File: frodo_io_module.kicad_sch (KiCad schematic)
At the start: 150 parts, among them J1 Conn_02x04_Top_Bottom, J10 JST-GH 4Pin, J11 JST-GH 4Pin, J14 Conn_02x03_Odd_Even, J16 USB_C_Receptacle_USB2.0, J17 TC2050, J2 Conn_02x10_Odd_Even, J3 Conn_02x04_Top_Bottom, J4 Conn_02x03_Odd_Even, J5 Conn_02x04_Odd_Even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

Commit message: more routing
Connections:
- net v_main_pre_sense is gone; now on net main_voltage: D13.1 (K), D14.1 (K)
- net AIN2: now also U3.25 (PC5); no longer U3.24 (PC4)
- net AIN3: now also U3.24 (PC4); no longer U3.25 (PC5)
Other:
- note added: "@todo: swaped AIN2 und AIN3 for better routing"
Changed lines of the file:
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@@
 		)
 	)
+	(text "@todo: swaped AIN2 und AIN3 for better routing"
+		(exclude_from_sim no)
+		(at 261.62 89.408 0)
+		(effects
+			(font
+				(size 1.27 1.27)
+			)
+		)
+	)
 	(text "Isense"
 		(exclude_from_sim no)
@@
 	(global_label "AIN3"
 		(shape input)
-		(at 299.72 82.55 180)
+		(at 299.72 80.01 180)
 		(fields_autoplaced yes)
 		(effects
@@
 		)
 		(property "Intersheetrefs" "${INTERSHEET_REFS}"
-			(at 292.5014 82.55 0)
+			(at 292.5014 80.01 0)
 			(effects
 				(font
@@
 	(global_label "AIN2"
 		(shape input)
-		(at 299.72 80.01 180)
+		(at 299.72 82.55 180)
 		(fields_autoplaced yes)
 		(effects
@@
 		)
 		(property "Intersheetrefs" "${INTERSHEET_REFS}"
-			(at 292.5014 80.01 0)
+			(at 292.5014 82.55 0)
 			(effects
 				(font
@@
 			)
 		)
-		(property "Value" "v_main_pre_sense"
+		(property "Value" "main_voltage"
 			(at 60.96 172.7199 90)
 			(effects

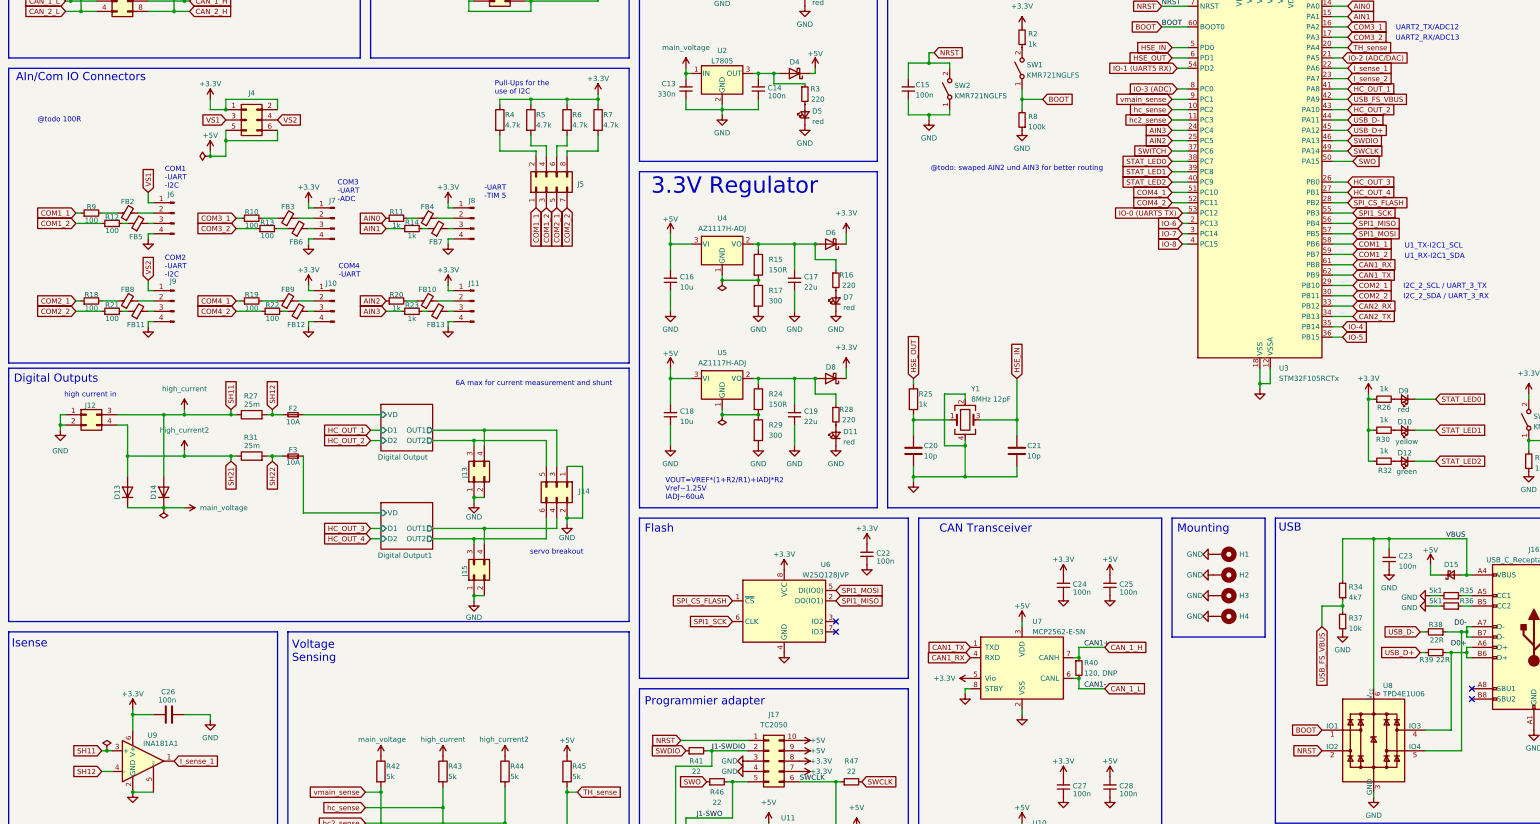
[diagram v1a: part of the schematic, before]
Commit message: remove second 3.3V reg and i2c pull up jumpers
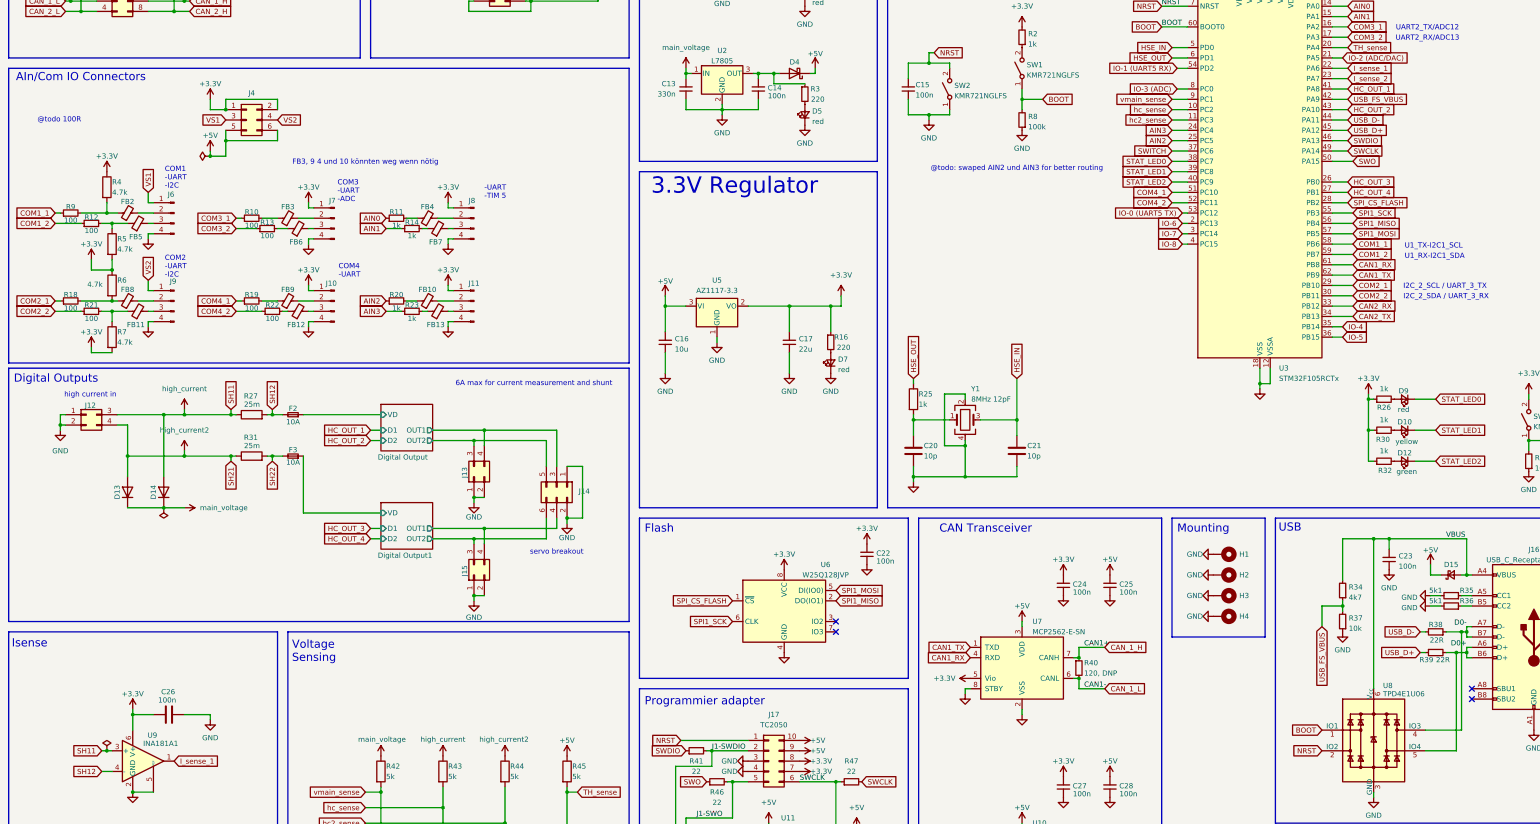
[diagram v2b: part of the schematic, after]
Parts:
- removed C18: 10u, Capacitor_SMD:C_0402_1005Metric, symbol Device:C_Small
- removed C19: 22u, Capacitor_SMD:C_0402_1005Metric, symbol Device:C_Small
- removed D11: red, LED_SMD:LED_0603_1608Metric, symbol Device:LED_Small
- removed D6, D8: RB070MM-30TR, Diode_SMD:D_SOD-123F, symbol Diode:SS34
- removed J5: Conn_02x04_Odd_Even, Connector_PinHeader_1.27mm:PinHeader_2x04_P1.27mm_Vertical_SMD, symbol Connector_Generic:Conn_02x04_Odd_Even
- removed R15, R24: 150R, Resistor_SMD:R_0402_1005Metric, symbol Device:R
- removed R17, R29: 300, Resistor_SMD:R_0402_1005Metric, symbol Device:R
- removed R28: 220, Resistor_SMD:R_0402_1005Metric, symbol Device:R_Small
- removed U4: AZ1117H-ADJ, Package_TO_SOT_SMD:SOT-223-3_TabPin2, symbol Regulator_Linear:AZ1117-3.3
- J14: footprint Connector_PinHeader_2.54mm:PinHeader_2x03_P2.54mm_Vertical_SMD -> Connector_PinHeader_2.54mm:PinHeader_2x03_P2.54mm_Vertical
- U5: value AZ1117H-ADJ -> AZ1117-3.3; LCSC C110475 -> C92102; Manufacturer Diodes Incorporated -> (none); Part# Diodes Incorporated AZ1117H-ADJTRG1 -> (none)
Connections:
- net +3.3V: now also C17.2, R16.1, R5.2, R7.2, U5.2 (VO); no longer R5.1, R7.1
- net D0+: now also U8.5 (IO4); no longer U8.4 (IO3)
- net D0-: now also U8.4 (IO3); no longer U8.5 (IO4)
- net GND: now also U5.1 (GND)
- net at R4.2: now also FB2.1, R9.2
- net at R6.2: now also FB8.1, R18.2
- net at FB11.1, R21.2: now also R7.1
- net at FB5.1, R12.2: now also R5.1
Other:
- note added: "FB3, 9 4 und 10 könnten weg wenn nötig"
- note removed: "Pull-Ups for the use of I2C"
- note removed: "VOUT=VREF*(1+R2/R1)+IADJ*R2 Vref~1.25V IADJ~60uA"
- moved on the sheet: C16, C17, D7, R12, R16, R18, R21, R4, R5, R6, R7, R9

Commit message: more routing
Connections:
- net AIN0: now also U3.23 (PA7); no longer U3.14 (PA0)
- net AIN1: now also U3.22 (PA6); no longer U3.15 (PA1)
- net I_sense_1: now also U3.14 (PA0); no longer U3.22 (PA6)
- net I_sense_2: now also U3.15 (PA1); no longer U3.23 (PA7)
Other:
- note added: "14, 15 mit 22, 23 getauscht"
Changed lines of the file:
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@@
 		)
 	)
+	(text "14, 15 mit 22, 23 getauscht"
+		(exclude_from_sim no)
+		(at 387.604 52.324 0)
+		(effects
+			(font
+				(size 1.27 1.27)
+			)
+		)
+	)
 	(text "COM3\n-UART\n-ADC"
 		(exclude_from_sim no)
@@
 	(global_label "I_sense_1"
 		(shape input)
-		(at 342.9 64.77 0)
+		(at 342.9 49.53 0)
 		(fields_autoplaced yes)
 		(effects
@@
 		)
 		(property "Intersheetrefs" "${INTERSHEET_REFS}"
-			(at 355.0171 64.77 0)
+			(at 355.0171 49.53 0)
 			(effects
 				(font
@@
 	(global_label "AIN1"
 		(shape input)
-		(at 342.9 52.07 0)
+		(at 342.9 64.77 0)
 		(fields_autoplaced yes)
 		(effects
@@
 		)
 		(property "Intersheetrefs" "${INTERSHEET_REFS}"
-			(at 350.1186 52.07 0)
+			(at 350.1186 64.77 0)
 			(effects
 				(font
@@
 	(global_label "AIN0"
 		(shape input)
-		(at 342.9 49.53 0)
+		(at 342.9 67.31 0)
 		(fields_autoplaced yes)
 		(effects
@@
 		)
 		(property "Intersheetrefs" "${INTERSHEET_REFS}"
-			(at 350.1186 49.53 0)
+			(at 350.1186 67.31 0)
 			(effects
 				(font
@@
 	(global_label "I_sense_2"
 		(shape input)
-		(at 342.9 67.31 0)
+		(at 342.9 52.07 0)
 		(fields_autoplaced yes)
 		(effects
@@
 		)
 		(property "Intersheetrefs" "${INTERSHEET_REFS}"
-			(at 355.0171 67.31 0)
+			(at 355.0171 52.07 0)
 			(effects
 				(font

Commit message: more routing
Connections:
- net COM4_1: now also U3.53 (PC12); no longer U3.51 (PC10)
- net COM4_2: now also U3.54 (PD2); no longer U3.52 (PC11)
- net GND: now also J2.17 (Pin_17); no longer J2.18 (Pin_18)
- net HC_OUT_1: now also U3.8 (PC0); no longer U3.41 (PA8)
- net HC_OUT_2: now also U3.4 (PC15); no longer U3.43 (PA10)
- net IO-0 (UART5 TX): now also J2.6 (Pin_6), U3.51 (PC10); no longer J2.5 (Pin_5), U3.53 (PC12)
- net IO-1 (UART5 RX): now also J2.4 (Pin_4), U3.52 (PC11); no longer J2.7 (Pin_7), U3.54 (PD2)
- net IO-2 (ADC/DAC): now also J2.8 (Pin_8); no longer J2.9 (Pin_9)
- net IO-3 (ADC): now also J2.14 (Pin_14), U3.41 (PA8); no longer J2.11 (Pin_11), U3.8 (PC0)
- net IO-4: now also J2.18 (Pin_18); no longer J2.15 (Pin_15)
- net IO-5: now also J2.16 (Pin_16); no longer J2.17 (Pin_17)
- net IO-6: now also J2.5 (Pin_5); no longer J2.12 (Pin_12)
- net IO-7: now also J2.7 (Pin_7); no longer J2.14 (Pin_14)
- net IO-8: now also J2.12 (Pin_12), U3.43 (PA10); no longer J2.16 (Pin_16), U3.4 (PC15)
- net SPI1_MISO: now also J2.15 (Pin_15); no longer J2.6 (Pin_6)
- net SPI1_MOSI: now also J2.9 (Pin_9); no longer J2.8 (Pin_8)
- net SPI1_SCK: now also J2.11 (Pin_11); no longer J2.4 (Pin_4)
- net hc2_sense: now also U3.10 (PC2); no longer U3.11 (PC3)
- net hc_sense: now also U3.11 (PC3); no longer U3.10 (PC2)
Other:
- note added: "@todo: swaped AIN2 und AIN3 for better routing swaped HC_OUT_2 with IO-2 and HC_OUT_1 with IO-8"
- note removed: "@todo: swaped AIN2 und AIN3 for better routing"

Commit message: finish routing
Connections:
- net GND: now also J2.15 (Pin_15); no longer J2.13 (Pin_13)
- net IO-4: now also J2.16 (Pin_16); no longer J2.18 (Pin_18)
- net IO-5: now also J2.18 (Pin_18); no longer J2.16 (Pin_16)
- net IO-6: now also J2.7 (Pin_7); no longer J2.5 (Pin_5)
- net IO-7: now also J2.5 (Pin_5); no longer J2.7 (Pin_7)
- net SPI1_MISO: now also J2.13 (Pin_13); no longer J2.15 (Pin_15)
- net SWCLK: no longer J17.6 (Pin_6), R47.1, U11.4 (IO3)
- new net J1-SWCLK: J17.6 (Pin_6), R47.1, U11.4 (IO3)
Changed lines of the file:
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@@
 	(wire
 		(pts
+			(xy 125.73 40.64) (xy 128.27 40.64)
+		)
+		(stroke
+			(width 0)
+			(type default)
+		)
+	)
+	(wire
+		(pts
 			(xy 31.75 50.8) (xy 35.56 50.8)
 		)
@@
 		)
 	)
-	(label "SWCLK"
-		(at 208.28 240.03 0)
+	(label "J1-SWCLK"
+		(at 209.55 240.03 0)
 		(effects
 			(font
@@
 	(global_label "IO-7"
 		(shape input)
-		(at 125.73 33.02 180)
+		(at 125.73 30.48 180)
 		(fields_autoplaced yes)
 		(effects
@@
 		)
 		(property "Intersheetrefs" "${INTERSHEET_REFS}"
-			(at 118.0276 33.02 0)
+			(at 118.0276 30.48 0)
 			(effects
 				(font
@@
 	(global_label "IO-6"
 		(shape input)
-		(at 125.73 30.48 180)
+		(at 125.73 33.02 180)
 		(fields_autoplaced yes)
 		(effects
@@
 		)
 		(property "Intersheetrefs" "${INTERSHEET_REFS}"
-			(at 118.0276 30.48 0)
+			(at 118.0276 33.02 0)
 			(effects
 				(font
@@
 	(global_label "IO-4"
 		(shape input)
-		(at 143.51 45.72 0)
+		(at 143.51 43.18 0)
 		(fields_autoplaced yes)
 		(effects
@@
 		)
 		(property "Intersheetrefs" "${INTERSHEET_REFS}"
-			(at 151.2124 45.72 0)
+			(at 151.2124 43.18 0)
 			(effects
 				(font
@@
 	(global_label "IO-5"
 		(shape input)
-		(at 143.51 43.18 0)
+		(at 143.51 45.72 0)
 		(fields_autoplaced yes)
 		(effects
@@
 		)
 		(property "Intersheetrefs" "${INTERSHEET_REFS}"
-			(at 151.2124 43.18 0)
+			(at 151.2124 45.72 0)
 			(effects
 				(font
@@
 	(global_label "SPI1_MISO"
 		(shape input)
-		(at 125.73 43.18 180)
+		(at 125.73 40.64 180)
 		(fields_autoplaced yes)
 		(effects
@@
 		)
 		(property "Intersheetrefs" "${INTERSHEET_REFS}"
-			(at 112.8872 43.18 0)
+			(at 112.8872 40.64 0)
 			(effects
 				(font
@@
 	(symbol
 		(lib_id "power:GND")
-		(at 128.27 40.64 270)
+		(at 125.73 43.18 270)
 		(unit 1)
 		(exclude_from_sim no)
@@
 		(fields_autoplaced yes)
 		(property "Reference" "#PWR013"
-			(at 121.92 40.64 0)
+			(at 119.38 43.18 0)
 			(effects
 				(font
@@
 		)
 		(property "Value" "GND"
-			(at 124.46 40.6399 90)
+			(at 121.92 43.1799 90)
 			(effects
 				(font
@@
 		)
 		(property "Footprint" ""
-			(at 128.27 40.64 0)
+			(at 125.73 43.18 0)
 			(effects
 				(font
@@
 		)
 		(property "Datasheet" ""
-			(at 128.27 40.64 0)
+			(at 125.73 43.18 0)
 			(effects
 				(font
@@
 		)
 		(property "Description" ""
-			(at 128.27 40.64 0)
+			(at 125.73 43.18 0)
 			(effects
 				(font

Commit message: added part numbers for all parts
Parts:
- J1, J12, J13, J14, J15, J17, J3, J4: LCSC# (none) -> x
- J2:  LCSC# (none) -> x
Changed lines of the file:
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@@
 			)
 		)
+		(property "LCSC#" "x"
+			(at 72.39 77.47 0)
+			(effects
+				(font
+					(size 1.27 1.27)
+				)
+				(hide yes)
+			)
+		)
 		(pin "3"
 		)
@@
 			)
 		)
+		(property "LCSC#" "x"
+			(at 128.27 165.1 0)
+			(effects
+				(font
+					(size 1.27 1.27)
+				)
+				(hide yes)
+			)
+		)
 		(pin "3"
 		)
@@
 			)
 		)
+		(property "LCSC#" "x"
+			(at 128.27 189.23 0)
+			(effects
+				(font
+					(size 1.27 1.27)
+				)
+				(hide yes)
+			)
+		)
 		(pin "3"
 		)
@@
 			)
 		)
+		(property "LCSC#" "x"
+			(at 148.59 167.64 90)
+			(effects
+				(font
+					(size 1.27 1.27)
+				)
+				(hide yes)
+			)
+		)
 		(pin "1"
 		)
@@
 			)
 		)
+		(property "LCSC#" "x"
+			(at 40.64 30.48 0)
+			(effects
+				(font
+					(size 1.27 1.27)
+				)
+				(hide yes)
+			)
+		)
 		(pin "6"
 		)
@@
 			)
 		)
+		(property "LCSC#" "x"
+			(at 33.02 149.86 0)
+			(effects
+				(font
+					(size 1.27 1.27)
+				)
+				(hide yes)
+			)
+		)
 		(pin "3"
 		)
@@
 			)
 		)
+		(property "LCSC#" "x"
+			(at 200.66 234.95 0)
+			(effects
+				(font
+					(size 1.27 1.27)
+				)
+				(hide yes)
+			)
+		)
 		(pin "7"
 		)
@@
 			)
 		)
+		(property " LCSC#" "x"
+			(at 133.35 35.56 0)
+			(effects
+				(font
+					(size 1.27 1.27)
+				)
+				(hide yes)
+			)
+		)
 		(pin "17"
 		)
@@
 			(at 40.64 45.72 0)
 			(effects
+				(font
+					(size 1.27 1.27)
+				)
+				(hide yes)
+			)
+		)
+		(property "LCSC#" "x"
+			(at 40.64 45.72 0)
+			(effects

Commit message: Fix ouput silkscreen number, clearance violation, start skew tuning (CAN)
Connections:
- net CAN_1_H renamed CAN_1+
- net CAN_1_L renamed CAN_1-
- net CAN_2_H renamed CAN_2+
- net CAN_2_L renamed CAN_2-
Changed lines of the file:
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@@
 		)
 	)
-	(global_label "CAN_1_L"
+	(global_label "CAN_1-"
 		(shape input)
 		(at 27.94 48.26 180)
@@
 		)
 		(property "Intersheetrefs" "${INTERSHEET_REFS}"
-			(at 17.0929 48.26 0)
+			(at 17.5162 48.26 0)
 			(effects
 				(font
@@
 		)
 	)
-	(global_label "CAN_2_L"
+	(global_label "CAN_2-"
 		(shape input)
 		(at 283.21 266.7 0)
@@
 		)
 		(property "Intersheetrefs" "${INTERSHEET_REFS}"
-			(at 294.0571 266.7 0)
+			(at 293.6338 266.7 0)
 			(effects
 				(font
@@
 		)
 	)
-	(global_label "CAN_2_L"
+	(global_label "CAN_2-"
 		(shape input)
 		(at 27.94 50.8 180)
@@
 		)
 		(property "Intersheetrefs" "${INTERSHEET_REFS}"
-			(at 17.0929 50.8 0)
+			(at 17.5162 50.8 0)
 			(effects
 				(font
@@
 		)
 	)
-	(global_label "CAN_1_L"
+	(global_label "CAN_1-"
 		(shape input)
 		(at 283.21 217.17 0)
@@
 		)
 		(property "Intersheetrefs" "${INTERSHEET_REFS}"
-			(at 294.0571 217.17 0)
-			(effects
-				(font
-					(size 1.27 1.27)
-				)
-				(justify left)
-				(hide yes)
-			)
-		)
-	)
-	(global_label "CAN_2_H"
+			(at 293.6338 217.17 0)
+			(effects
+				(font
+					(size 1.27 1.27)
+				)
+				(justify left)
+				(hide yes)
+			)
+		)
+	)
+	(global_label "CAN_2+"
 		(shape input)
 		(at 283.21 256.54 0)
@@
 		)
 		(property "Intersheetrefs" "${INTERSHEET_REFS}"
-			(at 294.3595 256.54 0)
+			(at 293.6338 256.54 0)
 			(effects
 				(font
@@
 		)
 	)
-	(global_label "CAN_1_H"
+	(global_label "CAN_1+"
 		(shape input)
 		(at 58.42 48.26 0)
@@
 		)
 		(property "Intersheetrefs" "${INTERSHEET_REFS}"
-			(at 69.5695 48.26 0)
+			(at 68.8438 48.26 0)
 			(effects
 				(font
@@
 		)
 	)
-	(global_label "CAN_2_H"
+	(global_label "CAN_2+"
 		(shape input)
 		(at 58.42 50.8 0)
@@
 		)
 		(property "Intersheetrefs" "${INTERSHEET_REFS}"
-			(at 69.5695 50.8 0)
+			(at 68.8438 50.8 0)
 			(effects
 				(font
@@
 		)
 	)
-	(global_label "CAN_1_H"
+	(global_label "CAN_1+"
 		(shape input)
 		(at 283.21 207.01 0)
@@
 		)
 		(property "Intersheetrefs" "${INTERSHEET_REFS}"
-			(at 294.3595 207.01 0)
-			(effects
-				(font
+			(at 293.6338 207.01 0)
+			(effects
+				(font

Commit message: started new design iteration, some scematic fixes (servo pwm&5v option, tsv issue)
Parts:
- removed FB11, FB12, FB2, FB3, FB5, FB6, FB8, FB9: BLM15PD121SN1D, Inductor_SMD:L_0402_1005Metric, symbol Device:FerriteBead_Small
- added JP1, JP2: SolderJumper_2_Open, Jumper:SolderJumper-2_P1.3mm_Open_RoundedPad1.0x1.5mm, symbol Jumper:SolderJumper_2_Open
- F2, F3: value 10A -> 5A; LCSC# C207003 -> C57525; Part# 0501010.WR1 -> 0466005.NRHF
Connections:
- net +5V: now also U8.6 (V_{cc}), JP1.2 (B), JP2.2 (B)
- net AIN0: now also U3.22 (PA6); no longer U3.23 (PA7)
- net AIN1: now also U3.21 (PA5); no longer U3.22 (PA6)
- net COM4_1: now also U3.51 (PC10); no longer U3.53 (PC12)
- net COM4_2: now also U3.52 (PC11); no longer U3.54 (PD2)
- net HC_OUT_1: now also U3.23 (PA7); no longer U3.8 (PC0)
- net HC_OUT_2: now also U3.41 (PA8); no longer U3.4 (PC15)
- net IO-0 (UART5 TX): now also U3.53 (PC12); no longer U3.51 (PC10)
- net IO-1 (UART5 RX): now also U3.54 (PD2); no longer U3.52 (PC11)
- net SH12: no longer F2.2
- net SH22: no longer F3.2
- net VBUS: no longer U8.6 (V_{cc})
- net high_current: now also F2.2; no longer R27.1, U9.3 (+)
- net high_current2: now also F3.2; no longer R31.1, U12.3 (+)
- net at R4.2, R9.2: now also J6.2 (Pin_2)
- net at R18.2, R6.2: now also J9.2 (Pin_2)
- net at R21.2, R7.1: now also J9.3 (Pin_3)
- net at R10.2: now also J7.2 (Pin_2)
- net at J10.2 (Pin_2): now also R19.2
- net at J10.3 (Pin_3): now also R22.2
- net at J7.3 (Pin_3): now also R13.2
- net at R12.2, R5.1: now also J6.3 (Pin_3)
- net Digital Output/VD renamed SH11
- net SH11: now also R27.1, U9.3 (+), JP2.1 (A)
- net Digital Output1/VD renamed SH21
- net SH21: now also R31.1, U12.3 (+), JP1.1 (A)
- net IO-2 (ADC/DAC) renamed IO-2
- net IO-2: now also U3.4 (PC15); no longer U3.21 (PA5)
- net IO-3 (ADC) renamed IO-3
- net IO-3: now also U3.43 (PA10); no longer U3.41 (PA8)
- net IO-8 renamed IO-8 (ADC)
- net IO-8 (ADC): now also U3.8 (PC0); no longer U3.43 (PA10)
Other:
- note added: "5A fused as fuses last ~5s at 200% current and >4h at nominal current"
- note added: "5v option, only use if corresponding fuse is soldered off!"
- note added: "@todo RC filter instead of farride beads?"
- note removed: "14, 15 mit 22, 23 getauscht"
- note removed: "@todo 100R"
- note removed: "@todo get single footprint"
- note removed: "@todo: swaped AIN2 und AIN3 for better routing swaped HC_OUT_2 with IO-2 and HC_OUT_1 with IO-8"
- note removed: "FB3, 9 4 und 10 könnten weg wenn nötig"
- moved on the sheet: D13, D14, F2, J10, J12, J6, J7, J9, R27, R31
